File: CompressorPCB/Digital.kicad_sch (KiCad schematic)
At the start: 46 parts, among them J2 SWD Header, J3 Header, J5 In, J6 Out, Q4 2N7002, SW2 RST, U6 NCS20074D, U7 STM32L052K6T6, U8 74HC595, U9 74HC595

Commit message: all routed, no DRC
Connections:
- net BYP_IN: now also U7.9 (PA3); no longer U7.18 (PA8)
- net FX_IN: now also J3.4 (Pin_4); no longer J3.2 (Pin_2)
- net FX_OUT: now also J3.2 (Pin_2); no longer J3.4 (Pin_4)
- net InJack: now also J3.3 (Pin_3); no longer J3.1 (Pin_1)
- net OutJack: now also J3.1 (Pin_1); no longer J3.3 (Pin_3)
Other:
- moved on the sheet: R56
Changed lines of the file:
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@@
 	)
 	(junction
-		(at 121.92 73.66)
-		(diameter 0)
-		(color 0 0 0 0)
-	)
-	(junction
 		(at 212.09 52.07)
 		(diameter 0)
@@
 	)
 	(junction
+		(at 121.666 60.96)
+		(diameter 0)
+		(color 0 0 0 0)
+	)
+	(junction
 		(at 259.08 95.25)
 		(diameter 0)
@@
 	)
 	(no_connect
+		(at 104.14 73.66)
+	)
+	(no_connect
 		(at 104.14 71.12)
 	)
@@
 	)
 	(no_connect
-		(at 104.14 60.96)
-	)
-	(no_connect
 		(at 104.14 66.04)
 	)
@@
 	(wire
 		(pts
-			(xy 213.36 161.29) (xy 223.52 161.29)
+			(xy 213.36 166.37) (xy 223.52 166.37)
 		)
 		(stroke
@@
 	(wire
 		(pts
-			(xy 121.92 73.66) (xy 124.46 73.66)
+			(xy 121.666 60.96) (xy 124.46 60.96)
 		)
 		(stroke
@@
 	(wire
 		(pts
-			(xy 213.36 163.83) (xy 214.63 163.83)
+			(xy 213.36 158.75) (xy 214.63 158.75)
 		)
 		(stroke
@@
 	(wire
 		(pts
+			(xy 104.14 60.96) (xy 121.666 60.96)
+		)
+		(stroke
+			(width 0)
+			(type default)
+		)
+	)
+	(wire
+		(pts
 			(xy 207.01 191.77) (xy 207.01 193.04)
 		)
@@
 	(wire
 		(pts
-			(xy 213.36 158.75) (xy 214.63 158.75)
+			(xy 213.36 163.83) (xy 214.63 163.83)
 		)
 		(stroke
@@
 	(wire
 		(pts
-			(xy 121.92 60.96) (xy 121.92 62.23)
+			(xy 121.666 47.244) (xy 121.666 48.514)
 		)
 		(stroke
@@
 	(wire
 		(pts
+			(xy 121.666 56.134) (xy 121.666 60.96)
+		)
+		(stroke
+			(width 0)
+			(type default)
+		)
+	)
+	(wire
+		(pts
 			(xy 184.15 49.53) (xy 190.5 49.53)
 		)
@@
 	(wire
 		(pts
-			(xy 104.14 73.66) (xy 121.92 73.66)
-		)
-		(stroke
-			(width 0)
-			(type default)
-		)
-	)
-	(wire
-		(pts
 			(xy 298.45 97.79) (xy 316.23 97.79)
 		)
@@
 	(wire
 		(pts
-			(xy 213.36 166.37) (xy 223.52 166.37)
+			(xy 213.36 161.29) (xy 223.52 161.29)
 		)
 		(stroke
@@
 	(wire
 		(pts
-			(xy 121.92 69.85) (xy 121.92 73.66)
-		)
-		(stroke
-			(width 0)
-			(type default)
-		)
-	)
-	(wire
-		(pts
 			(xy 35.56 172.72) (xy 35.56 180.34)
 		)
@@
 	)
 	(label "InJack"
-		(at 214.63 158.75 0)
+		(at 214.63 163.83 0)
 		(effects
 			(font
@@
 	)
 	(label "OutJack"
-		(at 214.63 163.83 0)
+		(at 214.63 158.75 0)
 		(effects
 			(font
@@
 	(global_label "FX_OUT"
 		(shape output)
-		(at 223.52 166.37 0)
+		(at 223.52 161.29 0)
 		(fields_autoplaced yes)
 		(effects
@@
 		)
 		(property "Intersheetrefs" "${INTERSHEET_REFS}"
-			(at 233.3995 166.37 0)
+			(at 233.3995 161.29 0)
 			(hide yes)
 			(show_name no)
@@
 	(global_label "FX_IN"
 		(shape output)
-		(at 223.52 161.29 0)
+		(at 223.52 166.37 0)
 		(fields_autoplaced yes)
 		(effects
@@
 		)
 		(property "Intersheetrefs" "${INTERSHEET_REFS}"
-			(at 231.7062 161.29 0)
+			(at 231.7062 166.37 0)
 			(hide yes)
 			(show_name no)
@@
 	(global_label "BYP_IN"
 		(shape input)
-		(at 124.46 73.66 0)
+		(at 124.46 60.96 0)
 		(fields_autoplaced yes)
 		(effects
@@
 		)
 		(property "Intersheetrefs" "${INTERSHEET_REFS}"
-			(at 133.9767 73.66 0)
+			(at 133.9767 60.96 0)
 			(hide yes)
 			(show_name no)
@@
 	(symbol
 		(lib_id "power:+3.3V")
-		(at 121.92 60.96 0)
+		(at 121.666 47.244 0)
 		(unit 1)
 		(body_style 1)
@@
 		(fields_autoplaced yes)
 		(property "Reference" "#PWR072"
-			(at 121.92 64.77 0)
+			(at 121.666 51.054 0)
 			(hide yes)
 			(show_name no)
@@
 		)
 		(property "Value" "+3.3V"
-			(at 121.92 56.515 0)
+			(at 121.666 42.799 0)
 			(show_name no)
 			(do_not_autoplace no)
@@
 		)
 		(property "Footprint" ""
-			(at 121.92 60.96 0)
+			(at 121.666 47.244 0)
 			(hide yes)
 			(show_name no)
@@
 		)
 		(property "Datasheet" ""
-			(at 121.92 60.96 0)
+			(at 121.666 47.244 0)
 			(hide yes)
 			(show_name no)
@@
 		)
 		(property "Description" ""
-			(at 121.92 60.96 0)
+			(at 121.666 47.244 0)
 			(hide yes)
 			(show_name no)
@@
 	(symbol
 		(lib_id "Device:R_US")
-		(at 121.92 66.04 0)
+		(at 121.666 52.324 0)
 		(unit 1)
 		(body_style 1)
@@
 		(fields_autoplaced yes)
 		(property "Reference" "R56"
-			(at 123.952 64.77 0)
+			(at 123.698 51.054 0)
 			(show_name no)
 			(do_not_autoplace no)
@@
 		)
 		(property "Value" "47k"
-			(at 123.952 67.31 0)
+			(at 123.698 53.594 0)
 			(show_name no)
 			(do_not_autoplace no)
@@
 		)
 		(property "Footprint" "Resistor_SMD:R_0805_2012Metric"
-			(at 122.936 66.294 90)
+			(at 122.682 52.578 90)
 			(hide yes)
 			(show_name no)
@@
 		)
 		(property "Datasheet" ""
-			(at 121.92 66.04 0)
+			(at 121.666 52.324 0)
 			(hide yes)
 			(show_name no)
@@
 		)
 		(property "Description" ""
-			(at 121.92 66.04 0)
+			(at 121.666 52.324 0)
 			(hide yes)
 			(show_name no)
@@
 		)
 		(property "MPN" "RK73B2ATTE473J"
-			(at 121.92 66.04 0)
+			(at 121.666 52.324 0)
 			(hide yes)
 			(show_name no)
@@
 		)
 		(property "Purchase Link" "https://www.mouser.com/en/ProductDetail/KOA-Speer/RK73B2ATTE473J?qs=sGAEpiMZZMtlubZbdhIBIAh9kdVoZFTe%2FhtWMi1uE0o%3D"
-			(at 121.92 66.04 0)
+			(at 121.666 52.324 0)
 			(hide yes)
 			(show_name no)
@@
 		)
 		(property "KLC_S3.3" ""
-			(at 121.92 66.04 0)
+			(at 121.666 52.324 0)
 			(hide yes)
 			(show_name no)
@@
 		)
 		(property "KLC_S4.1" ""
-			(at 121.92 66.04 0)
+			(at 121.666 52.324 0)
 			(hide yes)
 			(show_name no)

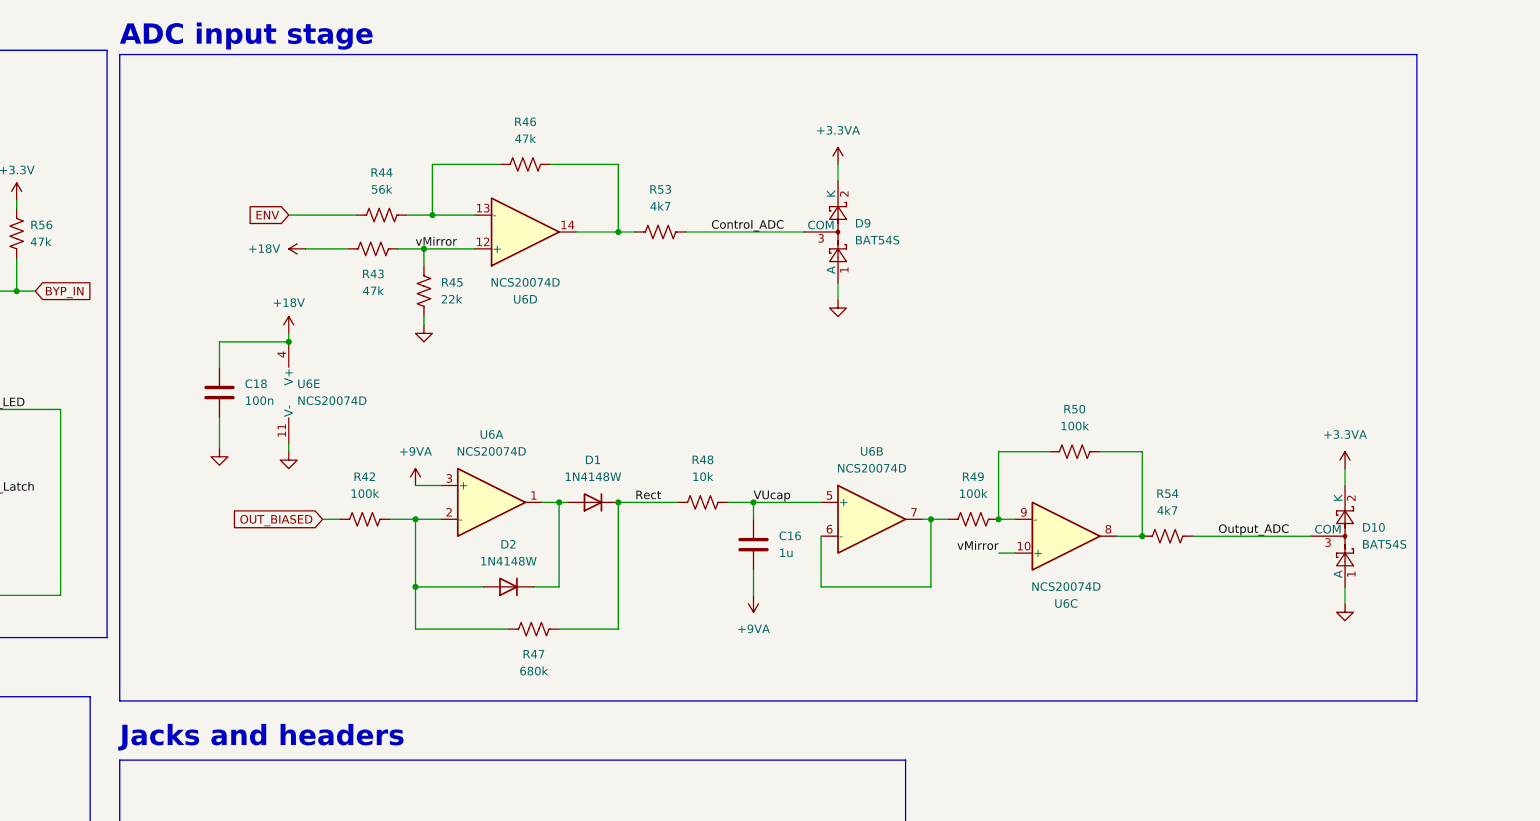
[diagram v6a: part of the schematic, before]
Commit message: updated env. follower and ADC driver in schem
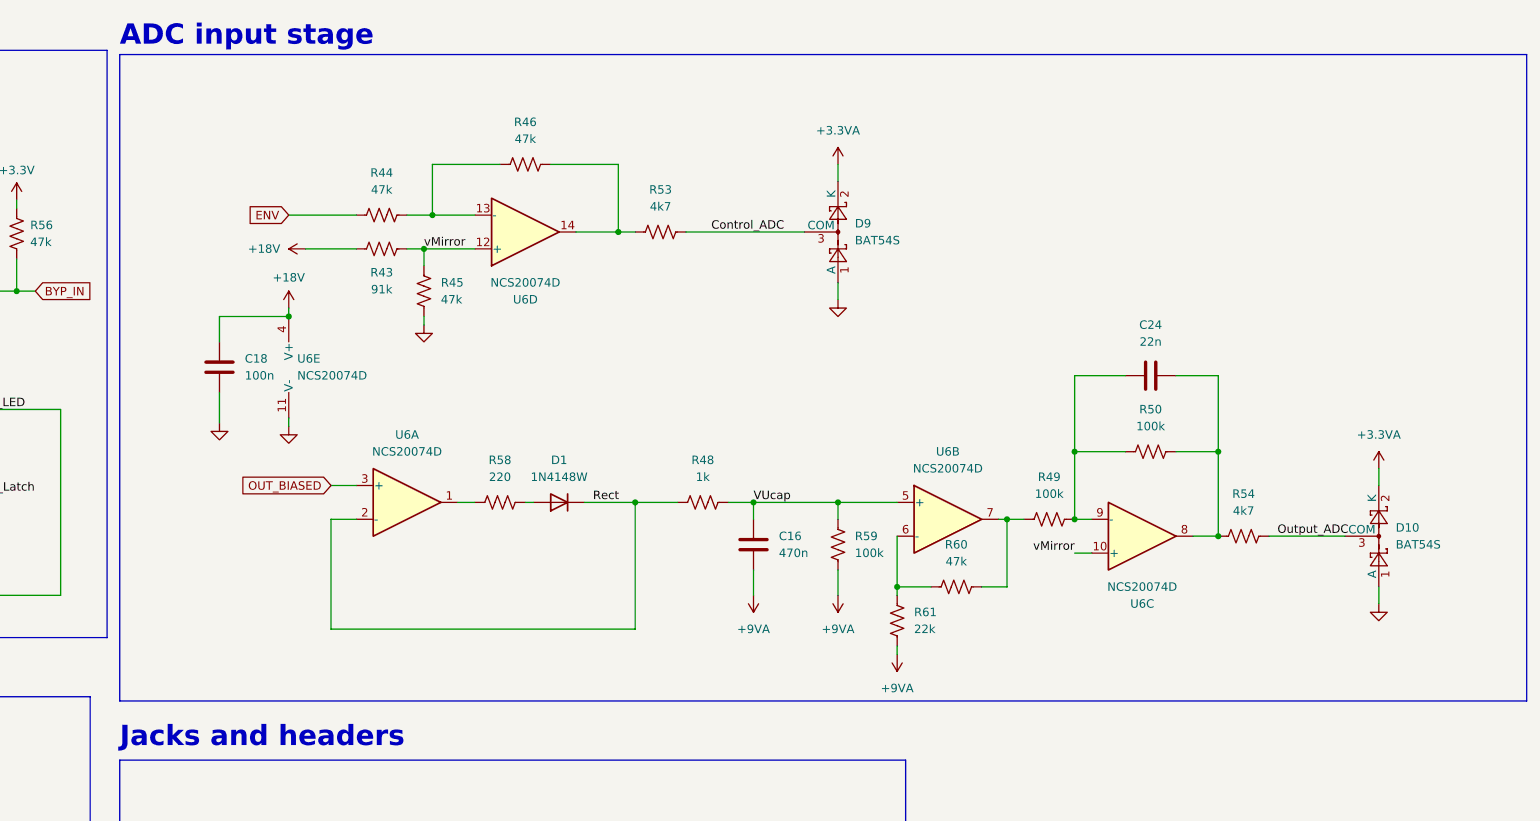
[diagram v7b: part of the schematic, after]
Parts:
- removed D2: 1N4148W, Diode_SMD:D_SOD-123, symbol Diode:1N4148W
- removed R42: 100k, Resistor_SMD:R_0805_2012Metric, symbol Device:R_US
- removed R47: 680k, Resistor_SMD:R_0805_2012Metric, symbol Device:R_US
- added C24: 22n, Capacitor_SMD:C_0805_2012Metric, symbol Device:C
- added R58: 220, Resistor_SMD:R_0805_2012Metric, symbol Device:R_US
- added R59: 100k, Resistor_SMD:R_0805_2012Metric, symbol Device:R_US
- added R60: 47k, Resistor_SMD:R_0805_2012Metric, symbol Device:R_US
- added R61: 22k, Resistor_SMD:R_0805_2012Metric, symbol Device:R_US
- C16: value 1u -> 470n
- R43: value 47k -> 91k
- R44: value 56k -> 47k
- R45: value 22k -> 47k
- R48: value 10k -> 1k
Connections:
- net +9VA: now also R59.1, R61.2; no longer U6.3 (+)
- net OUT_BIASED: now also U6.3 (+)
- net Rect: now also U6.2 (-)
- net VUcap: now also R59.2
- net at R50.2, R54.1, U6.8: now also C24.2
- net at R49.2, R50.1, U6.9 (-): now also C24.1
- net at U6.1: now also R58.1; no longer D1.2 (A)
- net at R49.1, U6.7: now also R60.1; no longer U6.6 (-)
- new net: D1.2 (A), R58.2
- new net: R60.2, R61.1, U6.6 (-)
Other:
- moved on the sheet: C18, D1, D10, R43, R49, R50, R54, U6A, U6B, U6C, U6E

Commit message: routing start
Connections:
- net OUT_BIASED: now also U6.10 (+); no longer U6.3 (+)
- net Rect: now also U6.9 (-); no longer U6.2 (-)
- net vMirror: now also U6.3 (+); no longer U6.10 (+)
- net at C24.2, R50.2, R54.1: now also U6.1; no longer U6.8
- net at C24.1, R49.2, R50.1: now also U6.2 (-); no longer U6.9 (-)
- net at R58.1: now also U6.8; no longer U6.1
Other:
- moved on the sheet: U6A, U6C
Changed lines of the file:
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@@
 	(symbol
 		(lib_id "Amplifier_Operational:NCS20074D")
-		(at 290.83 97.79 0)
-		(mirror x)
+		(at 180.34 92.71 0)
 		(unit 3)
 		(body_style 1)
@@
 		(dnp no)
 		(property "Reference" "U6"
-			(at 290.83 107.95 0)
+			(at 180.34 82.55 0)
 			(show_name no)
 			(do_not_autoplace no)
@@
 		)
 		(property "Value" "NCS20074D"
-			(at 290.83 105.41 0)
+			(at 180.34 85.09 0)
 			(show_name no)
 			(do_not_autoplace no)
@@
 		)
 		(property "Footprint" "Package_SO:SOIC-14_3.9x8.7mm_P1.27mm"
-			(at 293.37 97.79 0)
+			(at 182.88 92.71 0)
 			(hide yes)
 			(show_name no)
@@
 		)
 		(property "Datasheet" "https://www.onsemi.com/pub/Collateral/NCS20071-D.PDF"
-			(at 297.18 101.6 0)
+			(at 186.69 88.9 0)
 			(hide yes)
 			(show_name no)
@@
 		)
 		(property "Description" "Quad, 2.8V/µs, Rail-to-Rail Output, SOIC-14"
-			(at 290.83 97.79 0)
+			(at 180.34 92.71 0)
 			(hide yes)
 			(show_name no)
@@
 		)
 		(property "Sim.Library" "NCS2007X.MOD"
-			(at 290.83 97.79 0)
+			(at 180.34 92.71 0)
 			(hide yes)
 			(show_name no)
@@
 		)
 		(property "Sim.Name" "NCS2007_Quad"
-			(at 290.83 97.79 0)
+			(at 180.34 92.71 0)
 			(hide yes)
 			(show_name no)
@@
 		)
 		(property "Sim.Device" "SUBCKT"
-			(at 290.83 97.79 0)
+			(at 180.34 92.71 0)
 			(hide yes)
 			(show_name no)
@@
 		)
 		(property "Sim.Pins" "1=1 2=2 3=3 4=4 5=5 6=6 7=7 8=8 9=9 10=10 11=11 12=12 13=13 14=14"
-			(at 290.83 97.79 0)
+			(at 180.34 92.71 0)
 			(hide yes)
 			(show_name no)
@@
 	(symbol
 		(lib_id "Amplifier_Operational:NCS20074D")
-		(at 180.34 92.71 0)
+		(at 290.83 97.79 0)
+		(mirror x)
 		(unit 1)
 		(body_style 1)
@@
 		(in_pos_files yes)
 		(dnp no)
-		(fields_autoplaced yes)
 		(property "Reference" "U6"
-			(at 180.34 82.55 0)
+			(at 290.83 107.95 0)
 			(show_name no)
 			(do_not_autoplace no)
@@
 		)
 		(property "Value" "NCS20074D"
-			(at 180.34 85.09 0)
+			(at 290.83 105.41 0)
 			(show_name no)
 			(do_not_autoplace no)
@@
 		)
 		(property "Footprint" "Package_SO:SOIC-14_3.9x8.7mm_P1.27mm"
-			(at 182.88 92.71 0)
+			(at 293.37 97.79 0)
 			(hide yes)
 			(show_name no)
@@
 		)
 		(property "Datasheet" "https://www.onsemi.com/pub/Collateral/NCS20071-D.PDF"
-			(at 186.69 88.9 0)
+			(at 297.18 101.6 0)
 			(hide yes)
 			(show_name no)
@@
 		)
 		(property "Description" "Quad, 2.8V/µs, Rail-to-Rail Output, SOIC-14"
-			(at 180.34 92.71 0)
+			(at 290.83 97.79 0)
 			(hide yes)
 			(show_name no)
@@
 		)
 		(property "Sim.Library" "NCS2007X.MOD"
-			(at 180.34 92.71 0)
+			(at 290.83 97.79 0)
 			(hide yes)
 			(show_name no)
@@
 		)
 		(property "Sim.Name" "NCS2007_Quad"
-			(at 180.34 92.71 0)
+			(at 290.83 97.79 0)
 			(hide yes)
 			(show_name no)
@@
 		)
 		(property "Sim.Device" "SUBCKT"
-			(at 180.34 92.71 0)
+			(at 290.83 97.79 0)
 			(hide yes)
 			(show_name no)
@@
 		)
 		(property "Sim.Pins" "1=1 2=2 3=3 4=4 5=5 6=6 7=7 8=8 9=9 10=10 11=11 12=12 13=13 14=14"
-			(at 180.34 92.71 0)
-			(hide yes)
-			(show_name no)
+			(at 290.83 97.79 0)
+			(hide yes)
+			(show_name no)
